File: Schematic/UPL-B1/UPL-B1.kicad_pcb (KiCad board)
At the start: 4 copper layers, 155 x 130 mm, 315 parts, among them K2 G5V-2_Split, P20 TestPoint, P21 TestPoint, P30 TestPoint, P31 TestPoint, P32 TestPoint, P33 TestPoint, P34 TestPoint, P40 TestPoint, P53 TestPoint, P54 TestPoint, P55 TestPoint, P56 TestPoint, P57 TestPoint, P58 TestPoint, X1 5102159-8, X2 Conn_01x03_Pin_Bridge, X3 Conn_01x06_Pin, X4 Conn_01x06_Pin, X50 Conn_01x03_Pin_Bridge, X51 Conn_01x03_Pin_Bridge, X52 Conn_01x03_Pin_Bridge

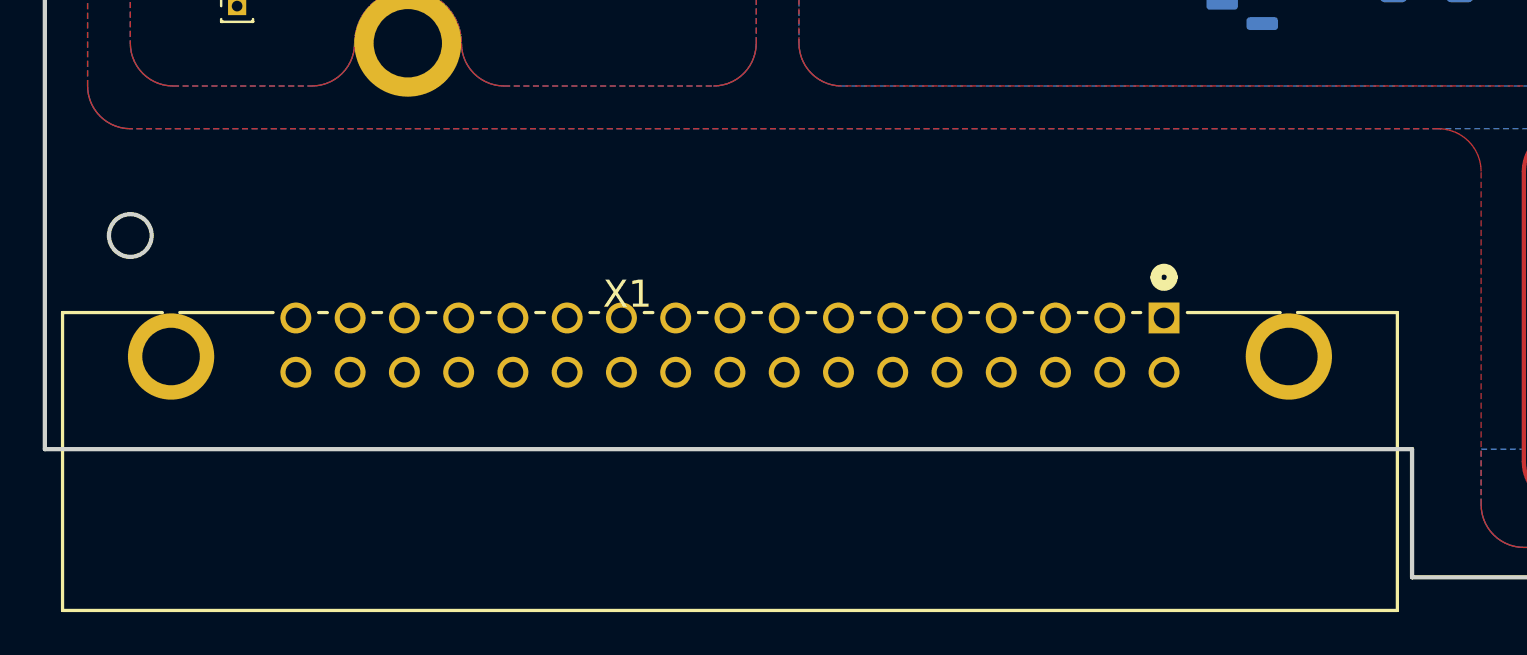
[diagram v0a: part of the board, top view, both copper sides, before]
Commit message: renamed sheets and updated main connector
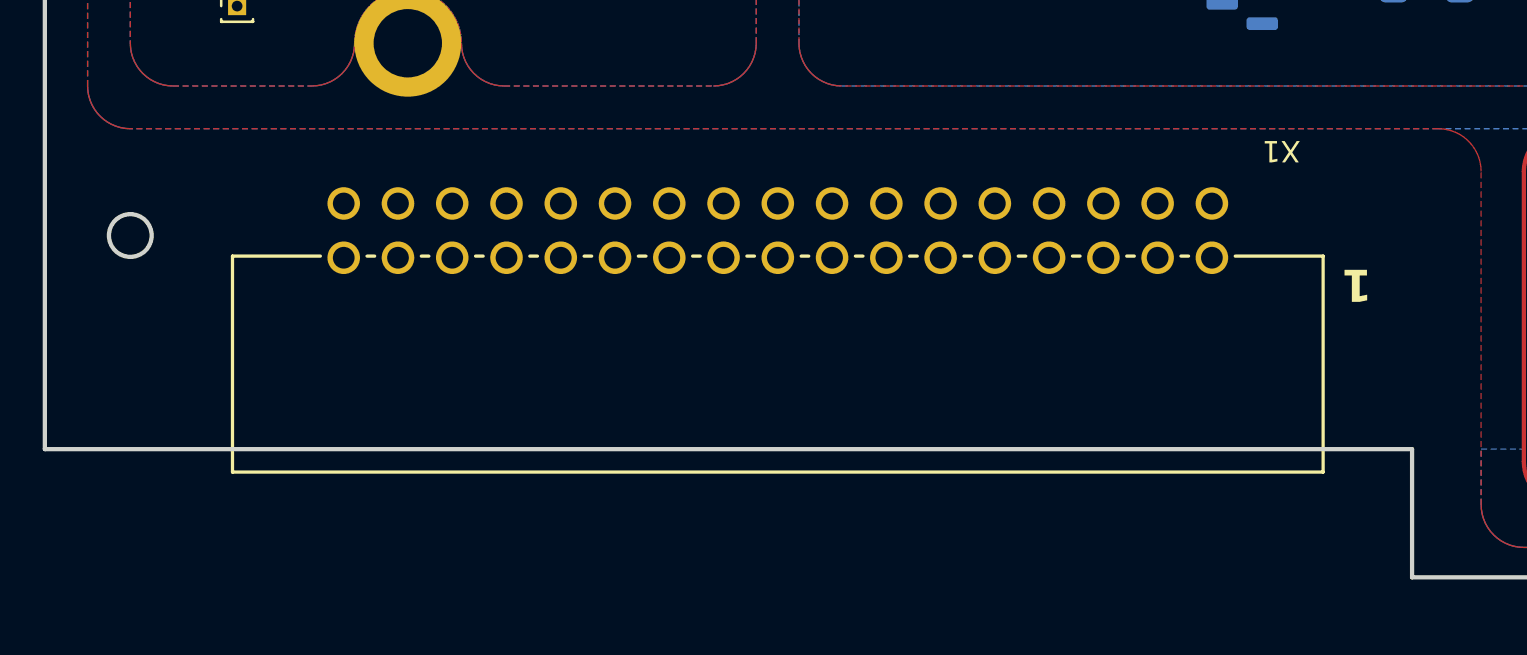
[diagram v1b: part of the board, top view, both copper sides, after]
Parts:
- X1: footprint UPL_B1:TYCO_5102159-8 -> UPL_B1:CONN_5103311-7_TYC
- moved X1 43.2 mm to (79.4, 134.9), turned to 180 degrees
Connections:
- net /Level Control (ALC)/LOFREQ renamed /Level Control (ALC)/LDFREQ
- C203 pad 1: +15V -> +15VA
- C204 pad 2: 15V -> -15VA
- C205 pad 1: +5V -> +5VA
- C207 pad 1: +5V -> +5VA
- C313 pad 1: +15V -> +15VA
- C314 pad 1: -15V -> -15VA
- C322 pad 2: -15V -> -VDC
- D20 pad 10: /Output IMD Attenuator/IN_CLK -> /IN_CLK
- D20 pad 13: /Output IMD Attenuator/~{IN_RD} -> //IN_RD
- D20 pad 4: /Output IMD Attenuator/~{IN_WR} -> //IN_WR
- D21 pad 11: /Output IMD Attenuator/FREQ_ENA -> /Level Control (ALC)/FREQ_ENA
- D21 pad 2: /Output IMD Attenuator/SDI -> /SDO
- D21 pad 6: /Output IMD Attenuator/LOFILT -> /Level Control (ALC)/LOFILT
- D21 pad 7: /Output IMD Attenuator/FILT -> /Level Control (ALC)/FILT
- D22 pad 10: Net-(D22-~{STB3}) -> Net-(D22-~{CLR})
- D22 pad 13: unconnected-(D22-~{CLR}-Pad13) -> Net-(D22-~{CLR})
- D22 pad 14: +5V -> +5VA
- D23 pad 9: /Output IMD Attenuator/SDO -> /SDI
- D30 pad 14: +5V -> +5VA
- D30 pad 9: /Integrator 1 & Loop Inverter/~{WR} -> /~{WR}
- D32 pad 14: +5V -> +5VA
- D32 pad 9: /Integrator 1 & Loop Inverter/~{WR} -> /~{WR}
- K2 pad 13: /Output IMD Attenuator/LOW DIST -> /LOW_DIST
- N31 pad 12: -15V -> -VDC
- N34 pad 4: -15V -> -15VA
- N34 pad 7: +15V -> +15VA
- N41 pad 12: -15V -> -VDC
- P21 pad 1: /Output IMD Attenuator/LOW DIST -> /LOW_DIST
- R203 pad 2: +15V -> +15VA
- R204 pad 2: 15V -> -15VA
- R205 pad 2: +5V -> +5VA
- R208 pad 1: Net-(D22-~{STB3}) -> Net-(D22-~{CLR})
- R208 pad 2: +5V -> +5VA
- R310 pad 1: +5V -> +5VA
- R341 pad 1: +5V -> +5VA
- R348 pad 1: -15V -> -VDC
- R410 pad 1: +5V -> +5VA
- X1 pad 10: /~{RD} -> //IN_RD
- X1 pad 12: /CLK -> /IN_CLK
- X1 pad 9: /~{WR} -> //IN_WR
